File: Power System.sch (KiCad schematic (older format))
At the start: 24 parts, among them U15 LMZ21701, U16 JST_Connector, U17 Switch_micromouse, U18 LMZ21701, U19 splitter, U24 Test_Point, U25 Test_Point, U26 Test_Point

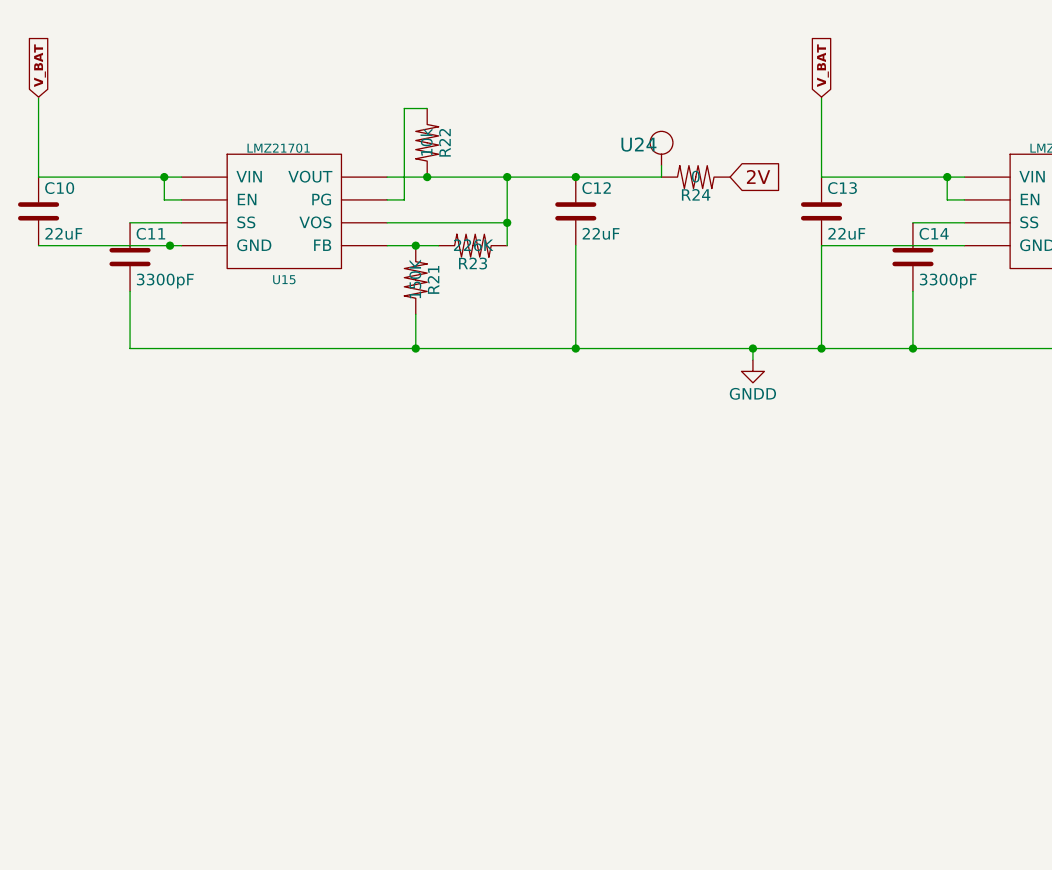
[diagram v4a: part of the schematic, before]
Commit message: added TPS61222DCK boost converter
-added TPS61222DCK boost converter for 5V input of the encoder
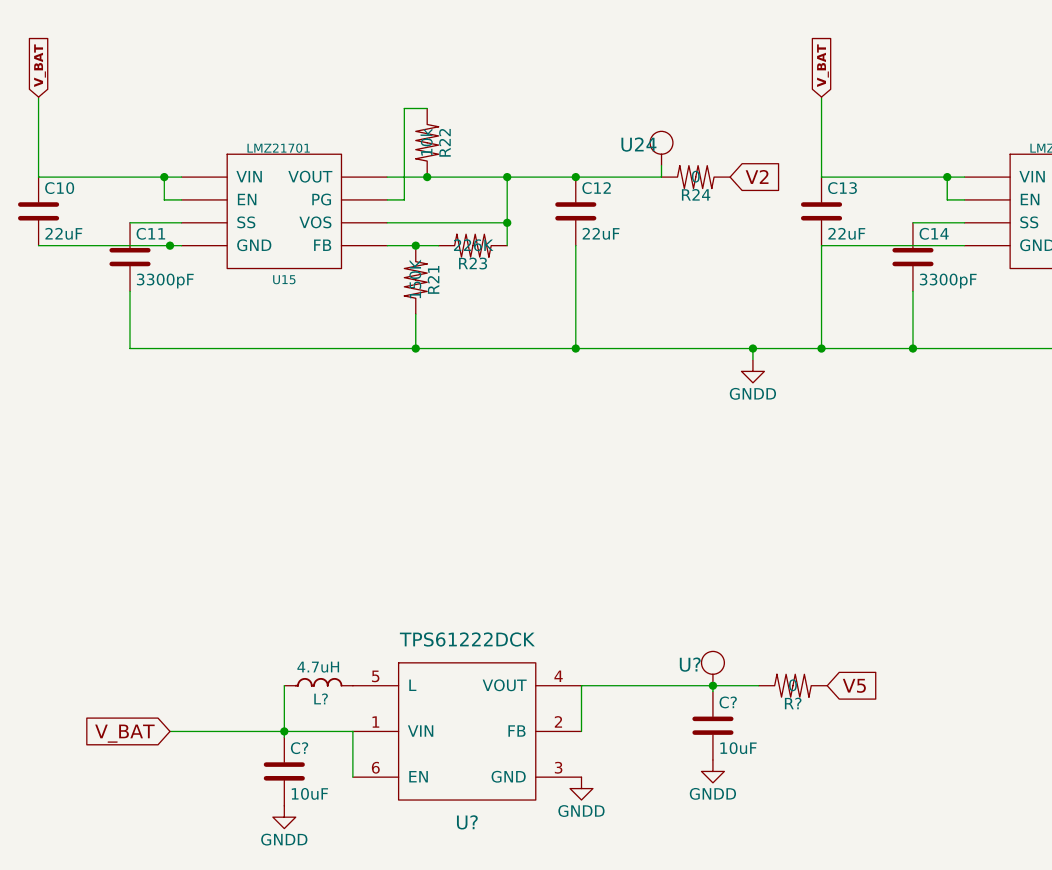
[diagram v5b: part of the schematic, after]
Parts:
- added C?: 10uF, Capacitors_SMD:C_0805, symbol C
- added C?: 10uF, Capacitors_SMD:C_0603, symbol C
- added L?: 4.7uH, symbol L
- added R?: 0, micromouse:R_0603, symbol R
- added U?: TPS61222DCK, micromouse:TPS61222DCK, symbol TPS61222DCK
- added U?: Test_Point, micromouse:Test_Point, symbol Test_Point
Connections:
- net GNDD: now also C?.2, C?.2, U?.3 (GND)
- net V_BAT: now also C?.1, L?.1, U?.1 (VIN), U?.6 (EN)
- net 2V renamed V2
- new net: C?.1, R?.2, U?.1, U?.2 (FB), U?.4 (VOUT)
- new net: L?.2, U?.5 (L)
- new net V5: R?.1
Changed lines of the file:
@@
 	7400 4550 7400 4625
 Text GLabel 3775 3800 2    60   Input ~ 0
-2V
+V2
 $Comp
 L C C12
@@
 	1    0    0    -1
 $EndComp
+$Comp
+L TPS61222DCK U?
+U 1 1 59F09F15
+P 2625 6225
+F 0 "U?" H 2625 5825 60  0000 C CNN
+F 1 "TPS61222DCK" H 2625 6625 60  0000 C CNN
+F 2 "micromouse:TPS61222DCK" H 2525 6225 60  0001 C CNN
+F 3 "" H 2525 6225 60  0001 C CNN
+F 4 "TPS61222DCK" H 2625 6325 60  0001 C CNN "manf#"
+	1    2625 6225
+	1    0    0    -1
+$EndComp
+$Comp
+L C C?
+U 1 1 59F0A09C
+P 3700 6200
+F 0 "C?" H 3725 6300 50  0000 L CNN
+F 1 "10uF" H 3725 6100 50  0000 L CNN
+F 2 "Capacitors_SMD:C_0805" H 3738 6050 50  0001 C CNN
+F 3 "" H 3700 6200 50  0000 C CNN
+F 4 "C0805C106K8PACTU" H 3700 6200 60  0001 C CNN "manf#"
+	1    3700 6200
+	1    0    0    -1
+$EndComp
+$Comp
+L C C?
+U 1 1 59F0A11D
+P 1825 6400
+F 0 "C?" H 1850 6500 50  0000 L CNN
+F 1 "10uF" H 1850 6300 50  0000 L CNN
+F 2 "Capacitors_SMD:C_0603" H 1863 6250 50  0001 C CNN
+F 3 "" H 1825 6400 50  0000 C CNN
+F 4 "GRM188R60J106ME47D" H 1825 6400 60  0001 C CNN "manf#"
+	1    1825 6400
+	1    0    0    -1
+$EndComp
+$Comp
+L L L?
+U 1 1 59F0A1A3
+P 2025 6025
+F 0 "L?" H 1985 5965 47  0000 C CNN
+F 1 "4.7uH" H 1975 6105 47  0000 C CNN
+F 2 "" V 1925 6025 50  0000 C CNN
+F 3 "" V 1925 6025 50  0000 C CNN
+F 4 "LQM2HPN4R7MGCL" H 2025 6025 60  0001 C CNN "manf#"
+	1    2025 6025
+	1    0    0    -1
+$EndComp
+Wire Wire Line
+	1325 6225 2125 6225
+Wire Wire Line
+	1825 6025 1825 6250
+Connection ~ 1825 6225
+Text GLabel 1325 6225 0    60   Input ~ 0
+V_BAT
+Wire Wire Line
+	2125 6225 2125 6425
+$Comp
+L GNDD #PWR?
+U 1 1 59F0A944
+P 1825 6550
+F 0 "#PWR?" H 1825 6300 50  0001 C CNN
+F 1 "GNDD" H 1825 6400 50  0000 C CNN
+F 2 "" H 1825 6550 50  0001 C CNN
+F 3 "" H 1825 6550 50  0001 C CNN
+	1    1825 6550
+	1    0    0    -1
+$EndComp
+$Comp
+L GNDD #PWR?
+U 1 1 59F0AAF3
+P 3700 6350
+F 0 "#PWR?" H 3700 6100 50  0001 C CNN
+F 1 "GNDD" H 3700 6200 50  0000 C CNN
+F 2 "" H 3700 6350 50  0001 C CNN
+F 3 "" H 3700 6350 50  0001 C CNN
+	1    3700 6350
+	1    0    0    -1
+$EndComp
+$Comp
+L GNDD #PWR?
+U 1 1 59F0AD12
+P 3125 6425
+F 0 "#PWR?" H 3125 6175 50  0001 C CNN
+F 1 "GNDD" H 3125 6275 50  0000 C CNN
+F 2 "" H 3125 6425 50  0001 C CNN
+F 3 "" H 3125 6425 50  0001 C CNN
+	1    3125 6425
+	1    0    0    -1
+$EndComp
+Wire Wire Line
+	3125 6225 3125 6025
+Wire Wire Line
+	3125 6025 3900 6025
+Wire Wire Line
+	3700 6025 3700 6050
+Text GLabel 4200 6025 2    60   Input ~ 0
+V5
+Connection ~ 3700 6025
+$Comp
+L Test_Point U?
+U 1 1 59F0B962
+P 3700 5925
+F 0 "U?" V 3710 5825 60  0000 C CNN
+F 1 "Test_Point" H 3710 6035 60  0001 C CNN
+F 2 "micromouse:Test_Point" H 3700 5925 60  0001 C CNN
+F 3 "" H 3700 5925 60  0001 C CNN
+	1    3700 5925
+	0    1    1    0
+$EndComp
+$Comp
+L R R?
+U 1 1 59F0BF87
+P 4050 6025
+F 0 "R?" V 4130 6025 50  0000 C CNN
+F 1 "0" V 4050 6025 50  0000 C CNN
+F 2 "micromouse:R_0603" V 3980 6025 50  0001 C CNN
+F 3 "" H 4050 6025 50  0001 C CNN
+	1    4050 6025
+	0    1    1    0
+$EndComp
 $EndSCHEMATC

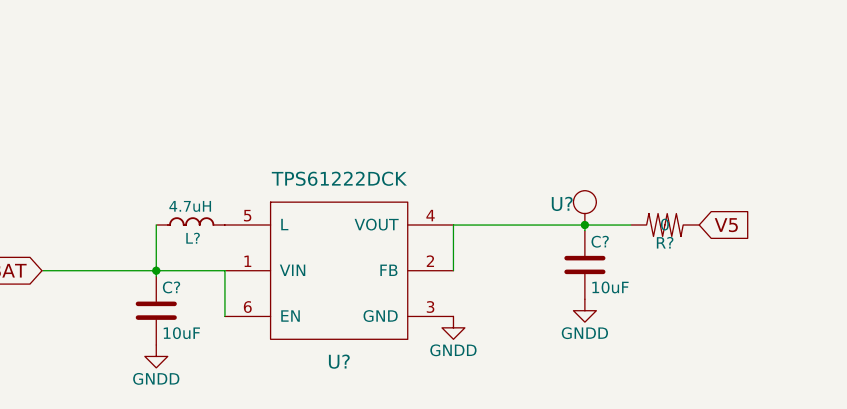
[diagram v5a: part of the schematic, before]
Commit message: layedout the boost converter
-layedout the boost converter
-rearranged the motor controller layout
-cuted some pcb from the center front to reduce the weight(lower weight higher turn speed)
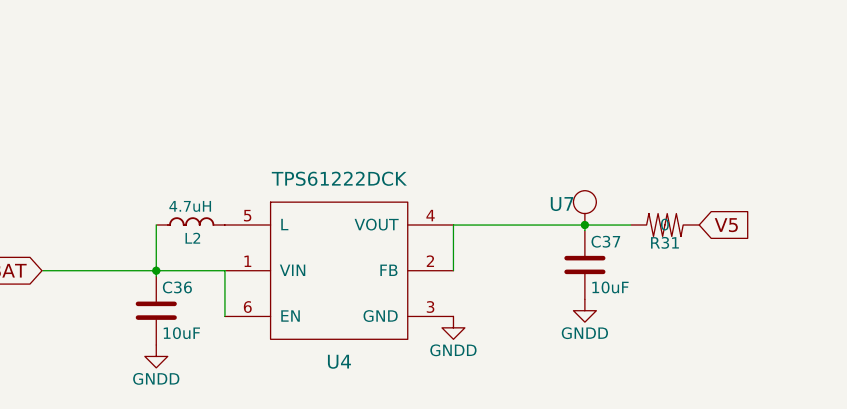
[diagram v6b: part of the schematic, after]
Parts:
- L2: renamed from L?; footprint (none) -> Inductors_NEOSID:Neosid_Inductor_SM-NE29_SMD1008
- gave numbers to parts that had none: 5
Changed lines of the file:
@@
 V_BAT
 $Comp
-L GNDD #PWR024
+L GNDD #PWR26
 U 1 1 59468675
 P 2825 2025
-F 0 "#PWR024" H 2825 1775 50  0001 C CNN
+F 0 "#PWR26" H 2825 1775 50  0001 C CNN
 F 1 "GNDD" H 2825 1875 50  0000 C CNN
 F 2 "" H 2825 2025 50  0001 C CNN
@@
 $EndComp
 $Comp
-L GNDD #PWR025
+L GNDD #PWR29
 U 1 1 59A9B990
 P 3875 4600
-F 0 "#PWR025" H 3875 4350 50  0001 C CNN
+F 0 "#PWR29" H 3875 4350 50  0001 C CNN
 F 1 "GNDD" H 3875 4450 50  0000 C CNN
 F 2 "" H 3875 4600 50  0001 C CNN
@@
 	2825 1900 2825 2025
 $Comp
-L GNDPWR #PWR026
+L GNDPWR #PWR25
 U 1 1 59AE8307
 P 2550 2025
-F 0 "#PWR026" H 2550 1825 50  0001 C CNN
+F 0 "#PWR25" H 2550 1825 50  0001 C CNN
 F 1 "GNDPWR" H 2550 1895 50  0000 C CNN
 F 2 "" H 2550 1975 50  0001 C CNN
@@
 	1150 4300 1150 4550
 $Comp
-L GNDA #PWR027
+L GNDA #PWR30
 U 1 1 59AE9CB5
 P 7400 4625
-F 0 "#PWR027" H 7400 4375 50  0001 C CNN
+F 0 "#PWR30" H 7400 4375 50  0001 C CNN
 F 1 "GNDA" H 7400 4475 50  0000 C CNN
 F 2 "" H 7400 4625 50  0001 C CNN
@@
 $EndComp
 $Comp
-L TPS61222DCK U?
+L TPS61222DCK U4
 U 1 1 59F09F15
 P 2625 6225
-F 0 "U?" H 2625 5825 60  0000 C CNN
+F 0 "U4" H 2625 5825 60  0000 C CNN
 F 1 "TPS61222DCK" H 2625 6625 60  0000 C CNN
 F 2 "micromouse:TPS61222DCK" H 2525 6225 60  0001 C CNN
@@
 $EndComp
 $Comp
-L C C?
+L C C37
 U 1 1 59F0A09C
 P 3700 6200
-F 0 "C?" H 3725 6300 50  0000 L CNN
+F 0 "C37" H 3725 6300 50  0000 L CNN
 F 1 "10uF" H 3725 6100 50  0000 L CNN
 F 2 "Capacitors_SMD:C_0805" H 3738 6050 50  0001 C CNN
@@
 $EndComp
 $Comp
-L C C?
+L C C36
 U 1 1 59F0A11D
 P 1825 6400
-F 0 "C?" H 1850 6500 50  0000 L CNN
+F 0 "C36" H 1850 6500 50  0000 L CNN
 F 1 "10uF" H 1850 6300 50  0000 L CNN
 F 2 "Capacitors_SMD:C_0603" H 1863 6250 50  0001 C CNN
@@
 $EndComp
 $Comp
-L L L?
+L L L2
 U 1 1 59F0A1A3
 P 2025 6025
-F 0 "L?" H 1985 5965 47  0000 C CNN
+F 0 "L2" H 1985 5965 47  0000 C CNN
 F 1 "4.7uH" H 1975 6105 47  0000 C CNN
-F 2 "" V 1925 6025 50  0000 C CNN
+F 2 "Inductors_NEOSID:Neosid_Inductor_SM-NE29_SMD1008" V 1925 6025 50  0001 C CNN
 F 3 "" V 1925 6025 50  0000 C CNN
 F 4 "LQM2HPN4R7MGCL" H 2025 6025 60  0001 C CNN "manf#"
@@
 	2125 6225 2125 6425
 $Comp
-L GNDD #PWR?
+L GNDD #PWR24
 U 1 1 59F0A944
 P 1825 6550
-F 0 "#PWR?" H 1825 6300 50  0001 C CNN
+F 0 "#PWR24" H 1825 6300 50  0001 C CNN
 F 1 "GNDD" H 1825 6400 50  0000 C CNN
 F 2 "" H 1825 6550 50  0001 C CNN
@@
 $EndComp
 $Comp
-L GNDD #PWR?
+L GNDD #PWR28
 U 1 1 59F0AAF3
 P 3700 6350
-F 0 "#PWR?" H 3700 6100 50  0001 C CNN
+F 0 "#PWR28" H 3700 6100 50  0001 C CNN
 F 1 "GNDD" H 3700 6200 50  0000 C CNN
 F 2 "" H 3700 6350 50  0001 C CNN
@@
 $EndComp
 $Comp
-L GNDD #PWR?
+L GNDD #PWR27
 U 1 1 59F0AD12
 P 3125 6425
-F 0 "#PWR?" H 3125 6175 50  0001 C CNN
+F 0 "#PWR27" H 3125 6175 50  0001 C CNN
 F 1 "GNDD" H 3125 6275 50  0000 C CNN
 F 2 "" H 3125 6425 50  0001 C CNN
@@
 Connection ~ 3700 6025
 $Comp
-L Test_Point U?
+L Test_Point U7
 U 1 1 59F0B962
 P 3700 5925
-F 0 "U?" V 3710 5825 60  0000 C CNN
+F 0 "U7" V 3710 5825 60  0000 C CNN
 F 1 "Test_Point" H 3710 6035 60  0001 C CNN
 F 2 "micromouse:Test_Point" H 3700 5925 60  0001 C CNN
@@
 $EndComp
 $Comp
-L R R?
+L R R31
 U 1 1 59F0BF87
 P 4050 6025
-F 0 "R?" V 4130 6025 50  0000 C CNN
+F 0 "R31" V 4130 6025 50  0000 C CNN
 F 1 "0" V 4050 6025 50  0000 C CNN
 F 2 "micromouse:R_0603" V 3980 6025 50  0001 C CNN

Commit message: Rev 1.0 done
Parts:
- C10: value 22uF -> 10uF; manf# JMK212BJ106KD-T -> GRM21BR60J106ME19L
- C12: manf# JMK212BJ226KG-T -> GRM21BC80G226ME39L
- C13: value 22uF -> 10uF; manf# (none) -> GRM21BR60J106ME19L
- C14: manf# (none) -> GRM033R70J332KA01D
- C15: manf# (none) -> GRM21BC80G226ME39L
- L1: manf# (none) -> BRL1608T100M
- R21: manf# ERJ-6ENF1503V -> CRCW0402150KFKED
- R22, R26: manf# (none) -> RC0402JR-0710KL
- R24, R28, R29, R31: manf# (none) -> RC0603JR-070RL
- R25: value 383k -> 180k; footprint micromouse:R_0402 -> micromouse:R_0603; manf# (none) -> RC0603FR-07180KL
- R27: value 1.21M -> 562k; manf# (none) -> CRCW0402562KFKED
- U15, U18: manf# LMZ21701SILT -> LMZ21701SILR
- U16, U17, U19: manf# (none) -> NONE
- U24, U25, U26, U7: manf# (none) -> RCU-0C
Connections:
- net GNDD: now also C10.2, U15.5 (GND)
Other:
- moved on the sheet: U19
